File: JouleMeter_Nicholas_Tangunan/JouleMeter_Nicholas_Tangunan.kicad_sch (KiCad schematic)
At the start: 0 parts

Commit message: placed all components and connections with labels for joulemeter project
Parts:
- added ADC: ADS1118QDGSRQ1, DGS0010A_N, symbol SMV_Custom:ADS1118QDGSRQ1
- added C1, C2, C4, C5, C6, C7, C8, C9: 0.1uF,50V, SMV_Passives:Cap0805, symbol SMV_Custom:C0805C104K5RACTU
- added C3: 0.33uF,50V, SMV_Passives:Cap0805, symbol SMV_Custom:C0805C334K5RACTU
- added CAN_Transceiver: MCP2562-E-P, Package_DIP:DIP-8_W7.62mm, symbol Interface_CAN_LIN:MCP2562-E-P
- added Current_Sense_Amp, Voltage_Buffer: INA193, Package_TO_SOT_SMD:SOT-23-5, symbol Amplifier_Current:INA193
- added DCDC_Converter: TSR0.5-2465, Converter_DCDC:Converter_DCDC_TRACO_TSR0.5-24xx_TSR0.5-24xxx_THT, symbol Regulator_Switching:TSR0.5-2465
- added FB1: FerriteBead, symbol Device:FerriteBead
- added J1, J2: 22035035, SMV_Connectors:3pin_CON_22035035_MOL, symbol SMV_Custom:3-pin Mini Molex Spox
- added LDO: ~, symbol SMV_Custom:AP7387-50FDCR-7
- added PowerIn/Out: 430450200, SMV_Connectors:CONN_SD-43045-001_02_MOL, symbol SMV_Custom:430450200
- added R1, R10, R2, R3, R4, R5, R6, R7, R8, R9: CRCW020149R9FNED, 50Ω, SMV_Passives:0805RESC2012X60N, symbol SMV_Custom:CRCW020149R9FNED
- added STM32: ~, symbol SMV_Custom:STM32_Nucleo_F446RE
- added SW1, SW2: SW_SPDT, symbol Switch:SW_SPDT
- added Shunt_R: 3.3mOhm, symbol Device:R_Shunt
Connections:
- new net: R10.1, R9.2, SW2.2 (B)
- new net: R4.2, R6.1, SW1.2 (B)
- new net: R3.2, R5.1, SW1.1 (A)
- new net: R7.1, R8.2, SW2.1 (A)
- new net: Voltage_Buffer.1, Voltage_Buffer.4 (-)
- new net +3v3: FB1.1, STM32.16 (+3V3)
- new net 5v+: C4.1, LDO.1 (VOUT), STM32.18 (+5V)
- new net Buck_Vin: DCDC_Converter.1 (Vin), PowerIn/Out.1
- new net Buck_Vout: C3.1, DCDC_Converter.3 (Vout), LDO.6 (VIN), Shunt_R.1
- new net GND: ADC.3 (GND), C1.2, C2.2, C3.2, C4.2, C6.2, C7.2, C8.2, Current_Sense_Amp.2 (GND), Current_Sense_Amp.3 (+), DCDC_Converter.2 (GND), J1.2, J2.2, LDO.4 (GND), PowerIn/Out.2, R1.1, R1.2, R10.2, R2.1, R2.2, R6.2, Shunt_R.4, Voltage_Buffer.2 (GND), Voltage_Buffer.3 (+)
- new net analog_in0: ADC.4 (AIN0), C2.1, C5.1, R3.1
- new net analog_in1: ADC.5 (AIN1), C5.2, C6.1, R4.1
- new net analog_in2: ADC.6 (AIN2), C7.1, C9.1, R8.1
- new net analog_in3: ADC.7 (AIN3), C8.1, C9.2, R9.1
- new net canh: CAN_Transceiver.7 (CANH), J1.1, J2.1
- new net canl: CAN_Transceiver.6 (CANL), J1.3, J2.3
- new net fb: CAN_Transceiver.5 (Vio), Current_Sense_Amp.5 (V+), FB1.2, R5.2, R7.2, Voltage_Buffer.5 (V+)
- new net gnd: CAN_Transceiver.8 (STBY), STM32.19 (GND)
- new net pa11: CAN_Transceiver.4 (RXD), STM32.52 (PA11)
- new net pa12: CAN_Transceiver.1 (TXD), STM32.50 (PA12)
- new net pa5: ADC.1 (SCLK), STM32.49 (PA5)
- new net pa6: ADC.9 (DOUT_DRDY_N), STM32.51 (PA6)
- new net pa7: ADC.10 (DIN), STM32.53 (PA7)
- new net pb6: ADC.2 (CS_N), STM32.55 (PB6)
- new net vdd: ADC.8 (VDD)
- new net voltage_measure: C1.1, CAN_Transceiver.3 (VDD), Current_Sense_Amp.1, Current_Sense_Amp.4 (-)

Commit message: updated schematic
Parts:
- removed C1: 0.1uF,50V, SMV_Passives:Cap0805, symbol SMV_Custom:C0805C104K5RACTU
- removed C3: 0.33uF,50V, SMV_Passives:Cap0805, symbol SMV_Custom:C0805C334K5RACTU
- removed CAN_Transceiver: MCP2562-E-P, Package_DIP:DIP-8_W7.62mm, symbol Interface_CAN_LIN:MCP2562-E-P
- removed Current_Sense_Amp, Voltage_Buffer: INA193, Package_TO_SOT_SMD:SOT-23-5, symbol Amplifier_Current:INA193
- removed DCDC_Converter: TSR0.5-2465, Converter_DCDC:Converter_DCDC_TRACO_TSR0.5-24xx_TSR0.5-24xxx_THT, symbol Regulator_Switching:TSR0.5-2465
- removed LDO: ~, symbol SMV_Custom:AP7387-50FDCR-7
- removed PowerIn/Out: 430450200, SMV_Connectors:CONN_SD-43045-001_02_MOL, symbol SMV_Custom:430450200
- removed SW1, SW2: SW_SPDT, symbol Switch:SW_SPDT
- removed Shunt_R: 3.3mOhm, symbol Device:R_Shunt
- added C1: 0.1uF,16V, SMV_Passives:Cap0805, symbol SMV_Custom:C0805C105K4RACTU
- added C10, C11, C12, C13: 0.47uF, SMV_Passives:CAPC340270_105N_KEM, symbol SMV_Custom:C1210C474K5RACTU
- added C14, C19: 0.1uF,50V, SMV_Passives:Cap0805, symbol SMV_Custom:C0805C104K5RACTU
- added C15, C16, C20, C3: 0.1uF, SMV_Passives:Cap0805, symbol SMV_Custom:C0805C104K5RACTU
- added C17, C22, C23: 10uF, SMV_Passives:Cap0805, symbol SMV_Custom:C0805C104K5RACTU
- added C18: 1uF,16V, SMV_Passives:Cap0805, symbol SMV_Custom:C0805C105K4RACTU
- added C21: 0.47 uF, SMV_Passives:Cap0805, symbol SMV_Custom:C0805C104K5RACTU
- added CAN_Transceiver1: MCP2562-E-P, Package_DIP:DIP-8_W7.62mm, symbol Interface_CAN_LIN:MCP2562-E-P
- added D1: LED, symbol Device:LED
- added J3, J5: XT60-M, SMV_Connectors:AMASS_XT60-M, symbol SMV_Custom:XT60-M
- added L1: 0.1 uF, symbol Device:L
- added R11, R14, R15: 50Ω, SMV_Passives:0805RESC2012X60N, symbol SMV_Custom:CRCW020149R9FNED
- added R12: 20Ω, SMV_Passives:0805RESC2012X60N, symbol SMV_Custom:CRCW020149R9FNED
- added R13: 600Ω, SMV_Passives:0805RESC2012X60N, symbol SMV_Custom:CRCW020149R9FNED
- added TP1: Ground, symbol Connector:TestPoint
- added TP10: Buck_VCC, symbol Connector:TestPoint
- added TP11: BUCK_FB, symbol Connector:TestPoint
- added TP2: CT_RCAN_H, symbol Connector:TestPoint
- added TP3: POWER-5V, symbol Connector:TestPoint
- added TP4: VF-V+, symbol Connector:TestPoint
- added TP5: VF-V-, symbol Connector:TestPoint
- added TP6: Current_OUT, symbol Connector:TestPoint
- added TP7: CT_RCAN_L, symbol Connector:TestPoint
- added TP8, TP9: TestPoint, symbol Connector:TestPoint
- added U1: LMR36510ADDA, Package_SO:Texas_HTSOP-8-1EP_3.9x4.9mm_P1.27mm_EP2.95x4.9mm_Mask2.4x3.1mm_ThermalVias, symbol Regulator_Switching:LMR36510ADDA
- added U2: ~, symbol SMV_Custom:UA78M05-Q1
- added U3: OP179GRT, Package_TO_SOT_SMD:SOT-23-5, symbol Amplifier_Operational:OP179GRT
- added U4: TMCS1126A1BQDVGR, SOIC10_DVG_TEX, symbol SMV_Custom:PMCS1126A1BQDVGR
- C4: value 0.1uF,50V -> 0.1uF
- J1: footprint SMV_Connectors:3pin_CON_22035035_MOL -> (none)
- R1, R10, R2, R3, R4, R5, R6, R7, R8, R9: value CRCW020149R9FNED, 50Ω -> 50Ω
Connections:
- net fb is gone; now on net +3V3: FB1.2, R5.2, R7.2
- net gnd is gone; now on net GND: STM32.19 (GND)
- net GND: now also C4.1, C1.2, C10.1, C10.2, C11.1, C11.2, C12.1, C12.2, C13.1, C13.2, C14.1, C15.2, C16.2, C17.2, C18.2, C19.2, C21.2, C22.2, C23.2, C3.2, CAN_Transceiver1.2 (VSS), CAN_Transceiver1.3 (VDD), CAN_Transceiver1.8 (STBY), D1.1 (K), J3.N (NEG), J3.P (POS), J5.N (NEG), J5.P (POS), R12.2, R13.1, R15.2, TP1.1, U1.1 (PGND), U1.2 (VIN), U1.3 (EN), U2.2 (COMMON), U2.4 (COMMON), U3.5 (V-), U4.1 (IN+), U4.2 (IN-), U4.7 (VREF), U4.9 (GND); no longer C4.2
- net at R10.1, R9.2: now also R7.1, R8.2
- net at R4.2, R6.1: now also R3.2, R5.1
- net +3v3 renamed +3V3
- net +3V3: now also C1.1, C18.1, C19.1, C3.1, CAN_Transceiver1.5 (Vio), U3.2 (V+), U4.4 (VS); no longer FB1.1
- net 5v+: no longer names the net of STM32.18 (+5V)
- net 5v+: no longer C4.1
- net canh renamed CAN_H
- net CAN_H: now also CAN_Transceiver1.7 (CANH), TP2.1
- net canl renamed CAN_L
- net CAN_L: now also CAN_Transceiver1.6 (CANL), TP7.1
- net pa11 renamed CAN-TXD
- net pa12 renamed CAN_RXD
- net CAN_RXD: now also CAN_Transceiver1.1 (TXD)
- net pa5 renamed SCLK
- net pa6 renamed CS_N
- net CS_N: now also ADC.2 (CS_N); no longer ADC.9 (DOUT_DRDY_N)
- net pa7 renamed DIN
- net pb6 renamed DOUT_DRDY_N
- net DOUT_DRDY_N: now also ADC.9 (DOUT_DRDY_N); no longer ADC.2 (CS_N)
- new net: C4.2, TP10.1, U1.6 (VCC)
- new net: TP6.1, U4.6 (VOUT)
- new net: C20.2, L1.1, U1.8 (SW)
- new net: R12.1, R13.2, TP4.1, U3.3 (+)
- new net: TP9.1, U1.4 (PG)
- new net: C20.1, TP8.1, U1.7 (BOOT)
- new net: D1.2 (A), R11.1
- new net +12V: C16.1, C17.1, C21.1, C22.1, C23.1, L1.2, R14.1, U2.1 (INPUT)
- new net +5V: C14.2, C15.1, R11.2, TP3.1, U2.3 (OUTPUT)
- new net CAN_TXD: CAN_Transceiver1.4 (RXD)
- new net FB: FB1.1, R14.2, R15.1, TP11.1, U1.5 (FB)
- new net Voltage_Follower: TP5.1, U3.1, U3.4 (-)
- no-connect marks 0 -> 61
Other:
- note added: "ADC"
- note added: "Buck Converter"
- note added: "CAN Transceiver 22035035 SMV_Connectors:3pin_CON_22035035_MOL"
- note added: "Current Hall Sensor"
- note added: "Ferrite Bead"
- note added: "LDO - 12V to 5V"
- note added: "STM32 Microcontroller"
- note added: "Voltage Divider"
- note added: "Voltage Follower"
- moved on the sheet: ADC, C2, C5, C6, C7, C8, C9, J1, J2, R1, R10, R2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

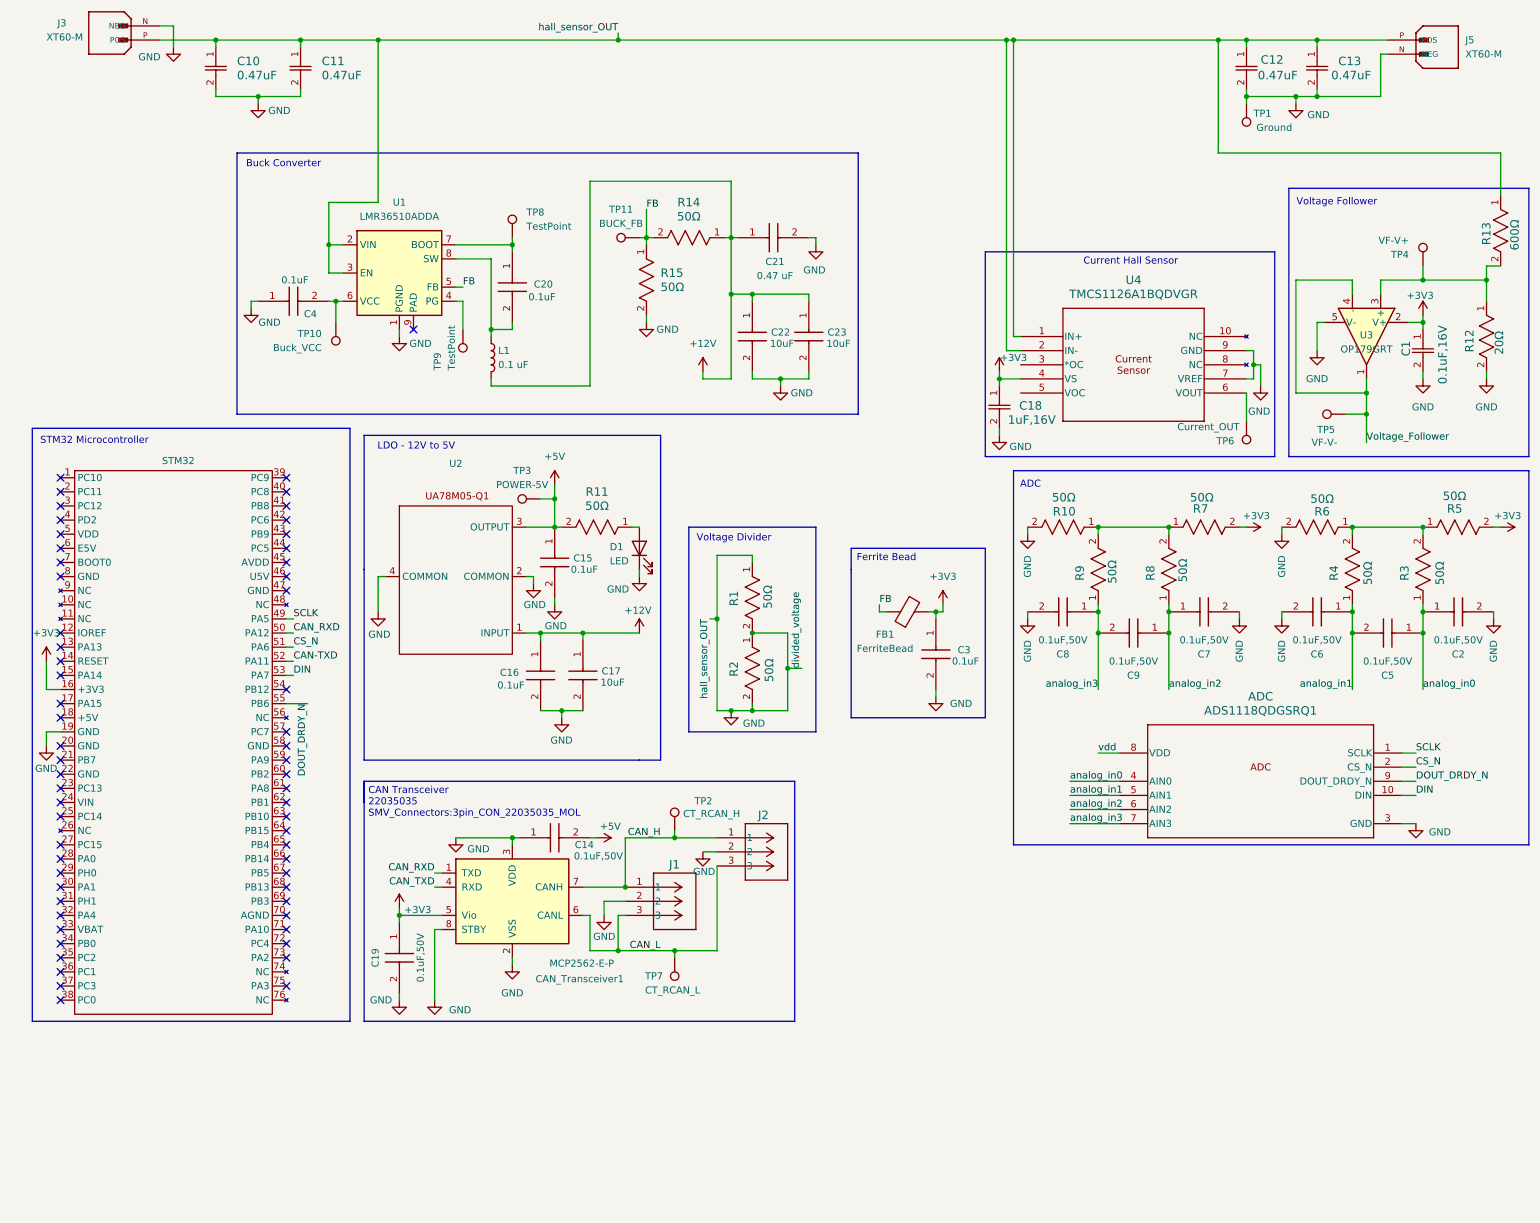
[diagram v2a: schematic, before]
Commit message: updated schematic based on 2nd round feedback
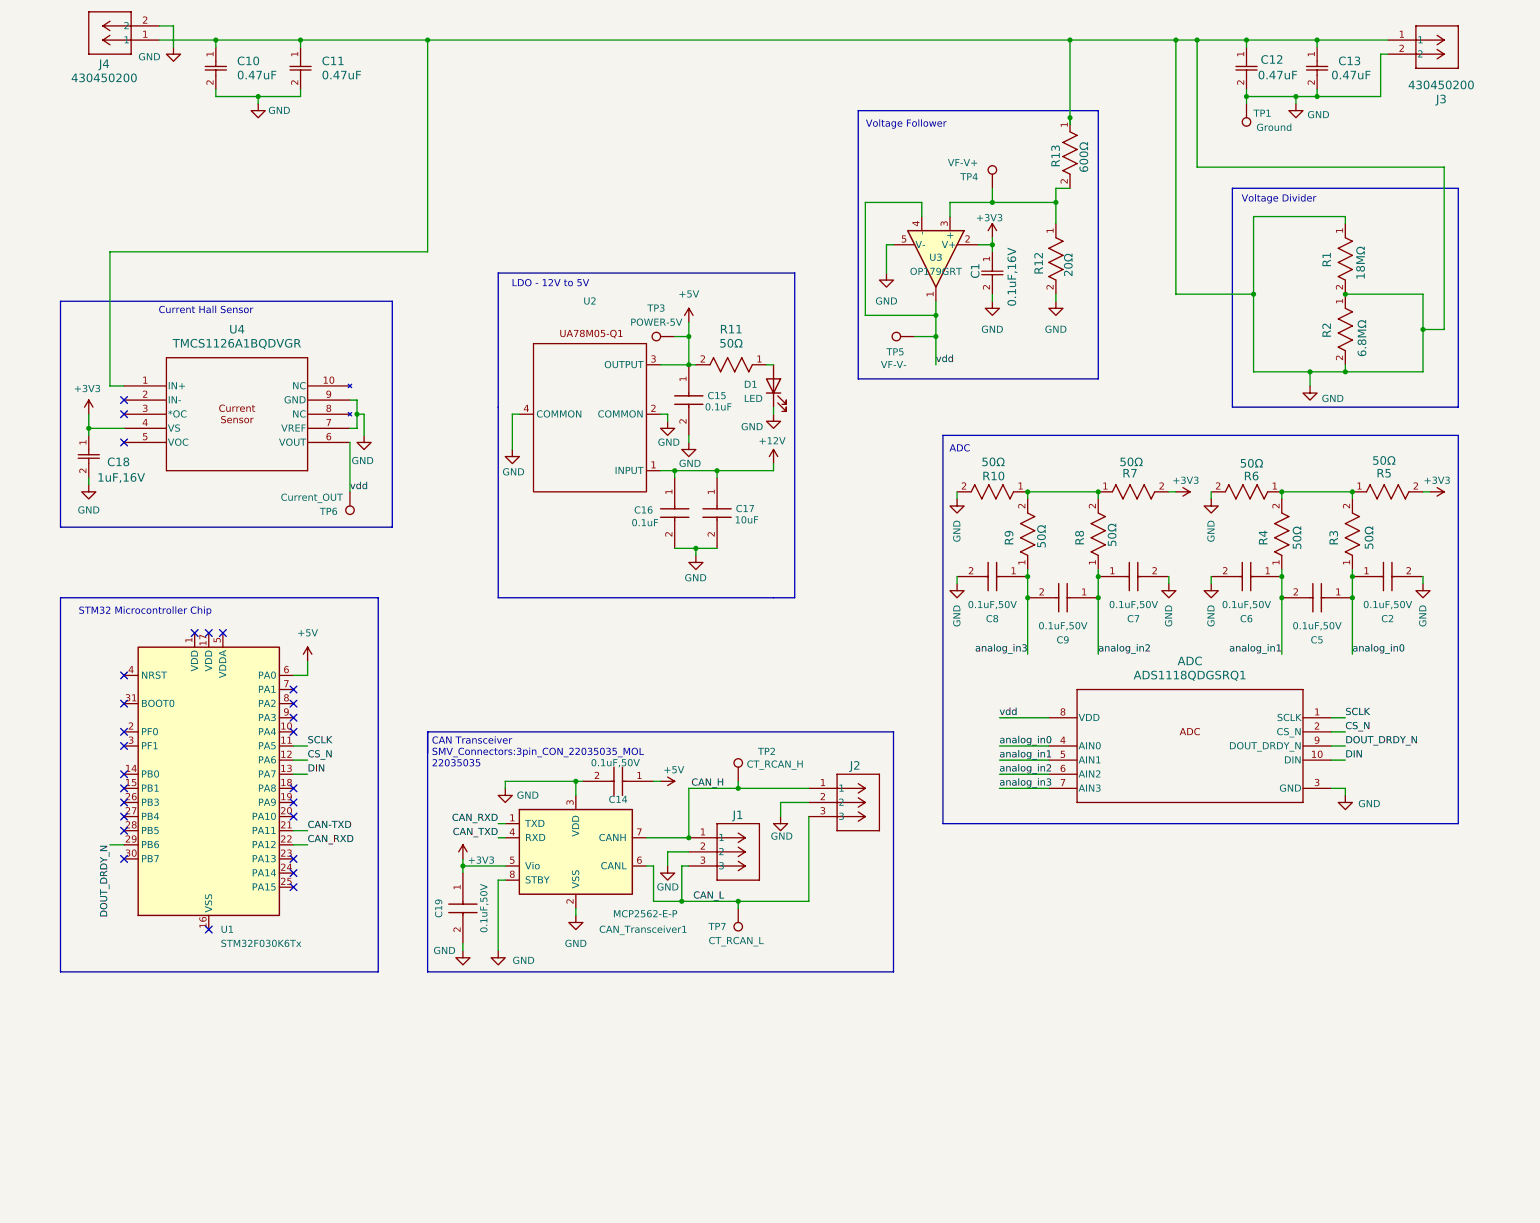
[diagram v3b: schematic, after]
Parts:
- removed C20, C3, C4: 0.1uF, SMV_Passives:Cap0805, symbol SMV_Custom:C0805C104K5RACTU
- removed C21: 0.47 uF, SMV_Passives:Cap0805, symbol SMV_Custom:C0805C104K5RACTU
- removed C22, C23: 10uF, SMV_Passives:Cap0805, symbol SMV_Custom:C0805C104K5RACTU
- removed FB1: FerriteBead, symbol Device:FerriteBead
- removed J3, J5: XT60-M, SMV_Connectors:AMASS_XT60-M, symbol SMV_Custom:XT60-M
- removed L1: 0.1 uF, symbol Device:L
- removed R14, R15: 50Ω, SMV_Passives:0805RESC2012X60N, symbol SMV_Custom:CRCW020149R9FNED
- removed STM32: ~, symbol SMV_Custom:STM32_Nucleo_F446RE
- removed TP10: Buck_VCC, symbol Connector:TestPoint
- removed TP11: BUCK_FB, symbol Connector:TestPoint
- removed TP8, TP9: TestPoint, symbol Connector:TestPoint
- removed U1: LMR36510ADDA, Package_SO:Texas_HTSOP-8-1EP_3.9x4.9mm_P1.27mm_EP2.95x4.9mm_Mask2.4x3.1mm_ThermalVias, symbol Regulator_Switching:LMR36510ADDA
- added J3, J4: 430450200, SMV_Connectors:CONN_SD-43045-001_02_MOL, symbol SMV_Custom:430450200
- added U1: STM32F030K6Tx, Package_QFP:LQFP-32_7x7mm_P0.8mm, symbol MCU_ST_STM32F0:STM32F030K6Tx
- R1: value 50Ω -> 18MΩ
- R2: value 50Ω -> 6.8MΩ
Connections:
- net Voltage_Follower is gone; now on net vdd: TP5.1, U3.1, U3.4 (-)
- net +5V: now also C14.1, U1.6 (PA0); no longer C14.2
- net CAN-TXD: now also U1.21 (PA11)
- net CAN_RXD: now also U1.22 (PA12)
- net CS_N: now also U1.12 (PA6)
- net DIN: now also U1.13 (PA7)
- net DOUT_DRDY_N: now also U1.29 (PB6)
- net GND: now also C14.2, J3.1, J3.2, J4.1, J4.2; no longer C14.1, U4.2 (IN-)
- net SCLK: now also U1.11 (PA5)
- net vdd: now also TP6.1, U4.6 (VOUT)
- new net: U1.16 (VSS), U1.32 (VSS)
- no-connect marks 61 -> 27
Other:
- note added: "CAN Transceiver SMV_Connectors:3pin_CON_22035035_MOL 22035035"
- note added: "STM32 Microcontroller Chip"
- note removed: "Buck Converter"
- note removed: "CAN Transceiver 22035035 SMV_Connectors:3pin_CON_22035035_MOL"
- note removed: "Ferrite Bead"
- note removed: "STM32 Microcontroller"
- moved on the sheet: ADC, C1, C14, C15, C16, C17, C18, C19, C2, C5, C6, C7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
